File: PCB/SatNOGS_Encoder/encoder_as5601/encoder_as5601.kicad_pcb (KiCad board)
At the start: 2 copper layers, 25 x 22.5 mm, 7 parts, among them P1 CONN_02X05, U1 AS5601

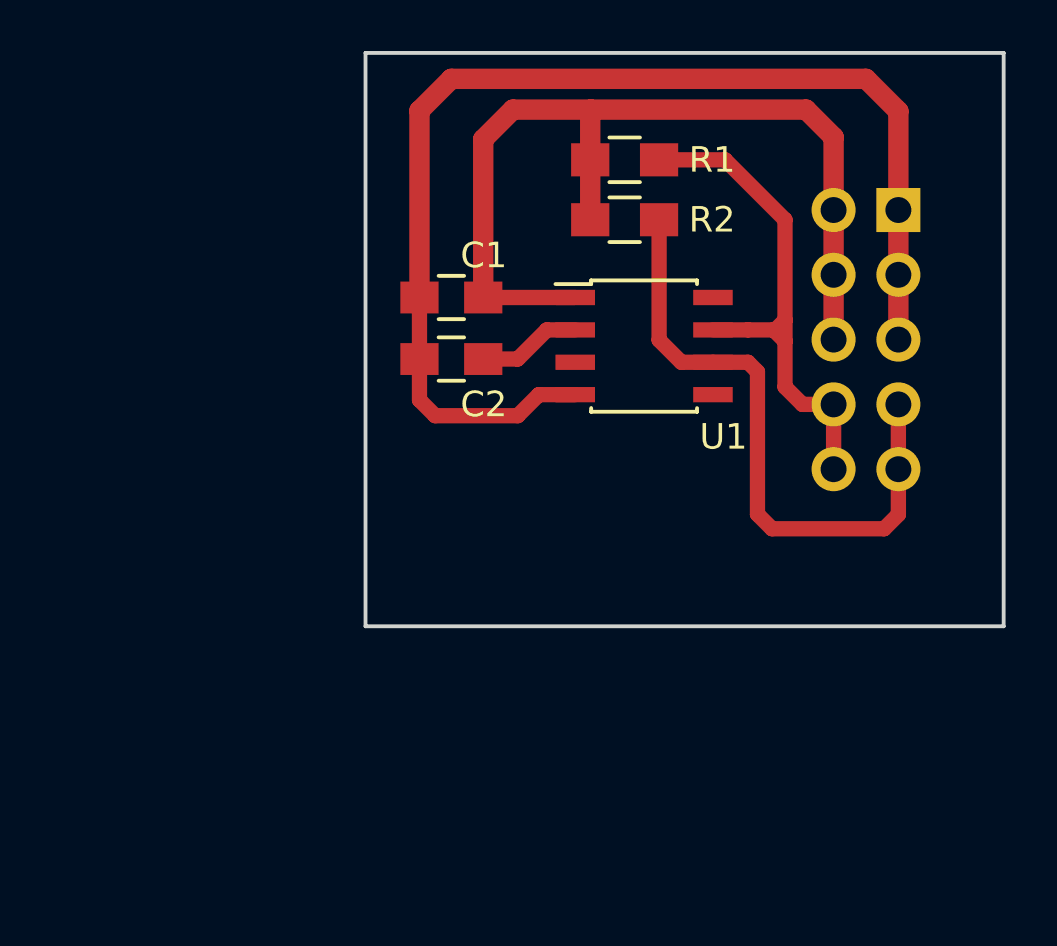
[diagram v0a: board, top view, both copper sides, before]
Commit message: Add reverse current protection and update pcb.
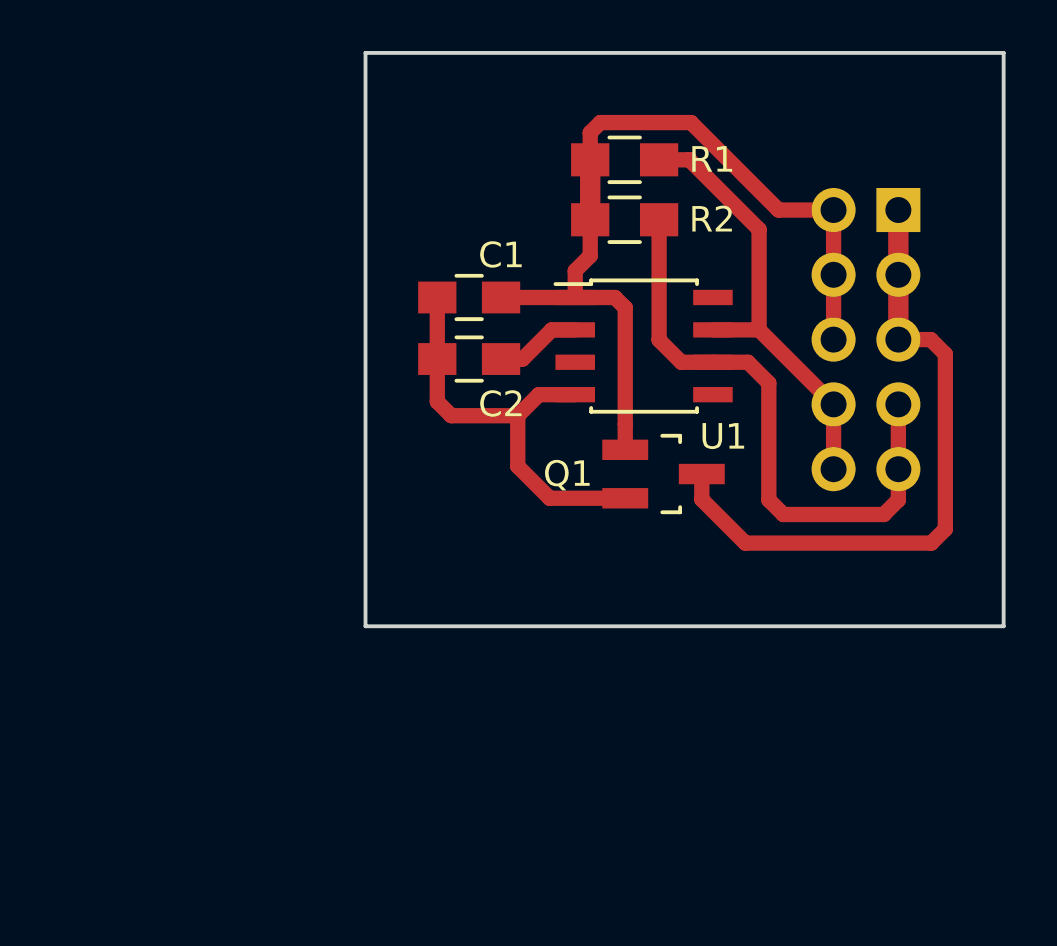
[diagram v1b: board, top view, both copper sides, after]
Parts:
- added Q1: Q_NMOS_GSD, TO_SOT_Packages_SMD:SOT-23_Handsoldering, F.Cu at (144.6, 85.2)
- moved C1 0.70 mm to (137.0, 78.2)
- moved C2 0.70 mm to (137.0, 80.6)
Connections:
- P1 pad 1: GND -> Net-(P1-Pad1)
- P1 pad 3: GND -> Net-(P1-Pad1)
- P1 pad 5: GND -> Net-(P1-Pad1)
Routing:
- net GND: track 46.8 -> 16.8 mm
- net Net-(P1-Pad1): track 0.00 -> 25.5 mm
- net /SCL: track 20.8 -> 17.5 mm
- net +5V: track 36.7 -> 33.5 mm
- net /SDA: track 25.0 -> 23.6 mm
- net Net-(C2-Pad1): track 4.08 -> 3.38 mm
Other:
- net class Default: trace_width 0.25 -> 0.6; via_dia 0.6 -> 0.8

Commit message: Update pcb to mount in cas.
Add mount holes.
Rearraange parts in order to place the AS5601 in the middle of PCB.
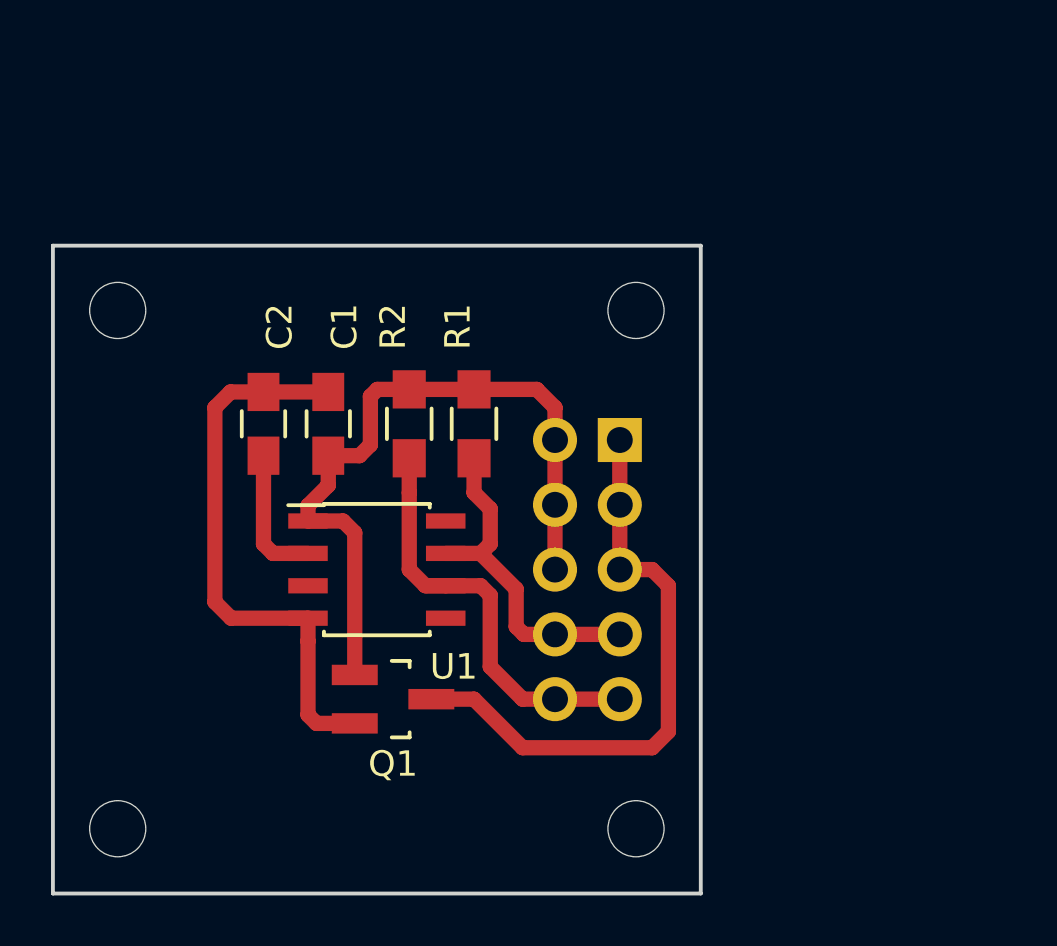
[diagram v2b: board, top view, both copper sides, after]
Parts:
- removed SatNOGS_Encoder: ©2016 Libre Space Foundation, Symbols:Symbol_OSHW-Logo_SilkScreen
- added REF**: MountingHole_2.2mm_M2, Mounting_Holes:MountingHole_2.2mm_M2, F.Cu at (123.2, 78.7)
- added REF**: MountingHole_2.2mm_M2, Mounting_Holes:MountingHole_2.2mm_M2, F.Cu at (123.2, 99.1)
- added REF**: MountingHole_2.2mm_M2, Mounting_Holes:MountingHole_2.2mm_M2, F.Cu at (143.5, 78.7)
- added REF**: MountingHole_2.2mm_M2, Mounting_Holes:MountingHole_2.2mm_M2, F.Cu at (143.5, 99.1)
- added ©2016 LSF: SatNOGS-Encoder, Symbols:OSHW-Logo2_7.3x6mm_SilkScreen, B.Cu at (128.9, 92.7)
- moved P1 14.2 mm to (142.9, 83.8)
- moved Q1 13.8 mm to (134.0, 94.0)
- moved U1 13.7 mm to (133.3, 88.9)
- moved R1 11.9 mm to (137.2, 83.2), turned to 270 degrees
- moved R2 11.6 mm to (134.6, 83.2), turned to 270 degrees
- moved C2 8.46 mm to (128.9, 83.2), turned to 90 degrees
- moved C1 7.42 mm to (131.4, 83.2), turned to 90 degrees
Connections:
- P1 pad 10: /SCL -> /SDA
- P1 pad 7: /SDA -> /SCL
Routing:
- net /SDA: track 23.6 -> 16.4 mm
- net +5V: track 33.5 -> 28.2 mm
- net GND: track 16.8 -> 22.0 mm
- net /SCL: track 17.5 -> 13.2 mm
- net Net-(P1-Pad1): track 25.5 -> 23.3 mm
- net Net-(C2-Pad1): track 3.38 -> 5.36 mm
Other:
- board size 25 x 22.5 mm -> 25.4 x 25.4 mm
- net class power added: clearance 0.2, trace_width 0.6, via_dia 0.8, via_drill 0.4
- net class signals added: clearance 0.2, trace_width 0.6, via_dia 0.8, via_drill 0.4
- board text added: "SCL"
- board text added: "SDA"
- board text removed: "SDA|SCL"
